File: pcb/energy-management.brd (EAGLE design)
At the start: 113.3 x 53.7 mm, 72 parts, among them J1 WIRE_HOLE-14AWG, J2 WIRE_HOLE-14AWG, J3 WIRE_HOLE-14AWG, J4 WIRE_HOLE-14AWG, U1 DS1307

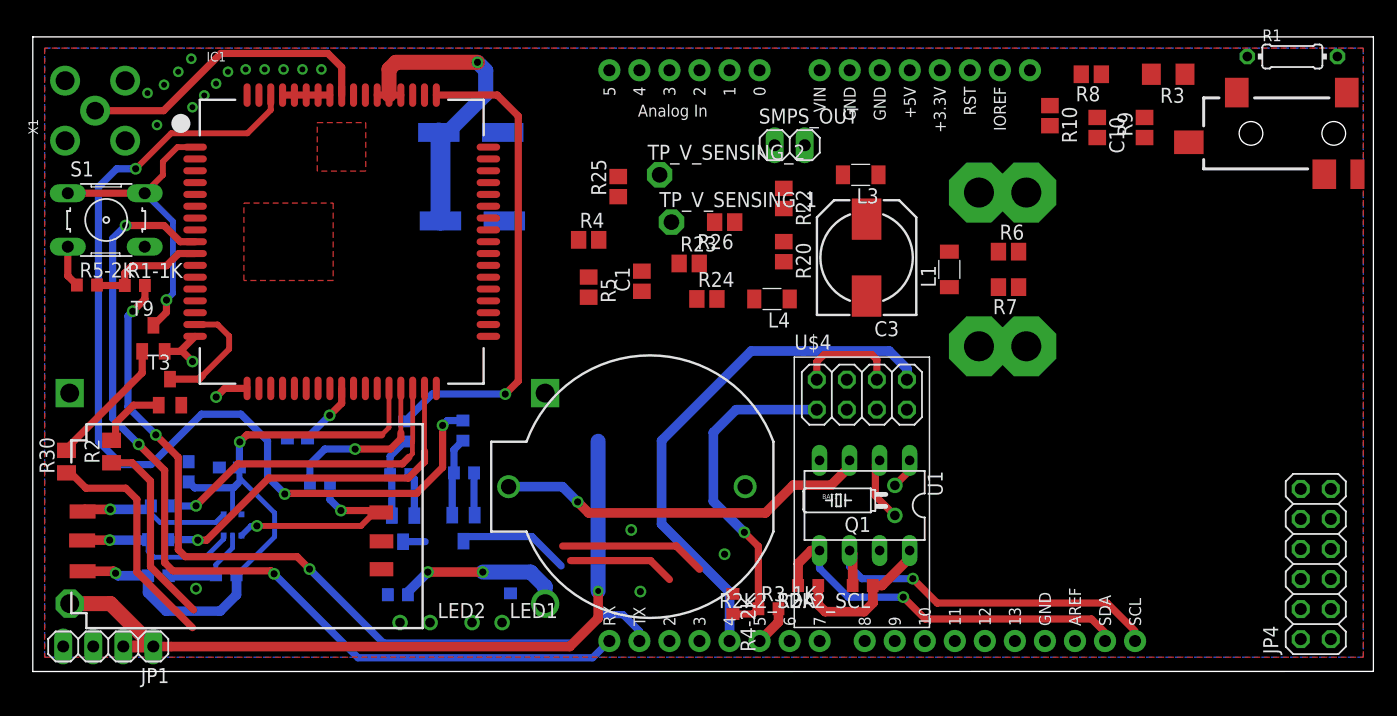
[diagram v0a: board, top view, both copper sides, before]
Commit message: added voltage and current measurement circuit
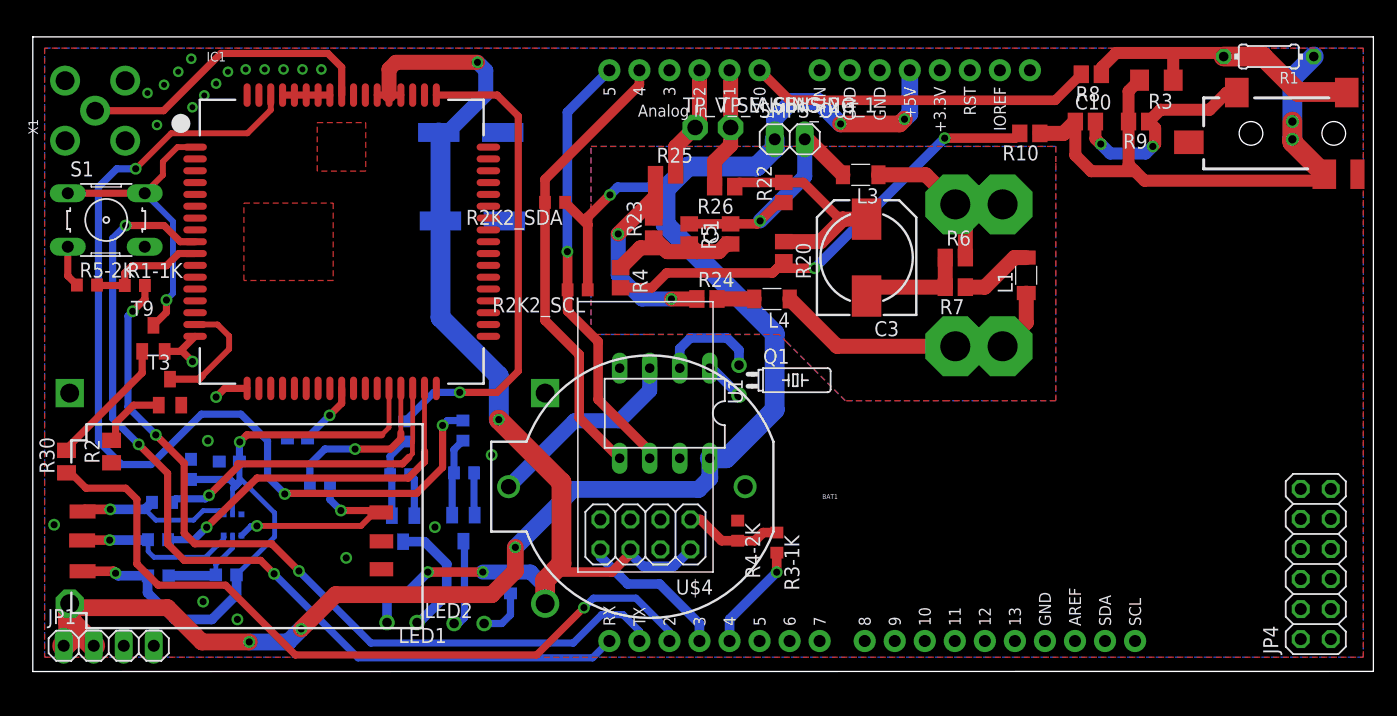
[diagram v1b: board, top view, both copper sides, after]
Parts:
- moved R2K2_SDA 38.8 mm to (44.2, 39.7)
- moved R2K2_SCL 34.7 mm to (46.1, 32.3)
- moved U$4 21.8 mm to (51.8, 11.6), turned to 180 degrees
- moved U1 18.6 mm to (53.4, 21.8)
- moved Q1 16.6 mm to (59.7, 24.6), turned to 270 degrees
- moved R5 9.62 mm to (55.5, 37.0)
- moved TP_V_SENSING_1 9.43 mm to (59.0, 46.0)
- moved C1 8.50 mm to (59.0, 37.0)
- moved L1 6.52 mm to (84.0, 33.5)
- moved R4-2K 6.21 mm to (59.6, 11.9)
- moved R3-1K 5.63 mm to (62.9, 10.9), turned to 270 degrees
- moved TP_V_SENSING_2 5.00 mm to (56.0, 46.0)
- moved R6 4.53 mm to (78.0, 35.0)
- moved R7 4.50 mm to (78.0, 32.5)
- moved R23 4.24 mm to (52.5, 37.5), turned to 90 degrees
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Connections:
- removed net 5V: SMPS_OUT.1
- net CTRL_SW1: no longer U$1.D8
- net CTRL_SW10: no longer U$1.D13
- net CTRL_SW2: no longer U$1.D9
- net CTRL_SW3: no longer U$1.D3
- net CTRL_SW4: no longer U$1.D2
- net CTRL_SW5: no longer U$1.A3
- net CTRL_SW6: no longer U$1.D7
- net CTRL_SW7: no longer U$1.D6
- net CTRL_SW8: no longer U$1.D12
- net CTRL_SW9: no longer U$1.D11
- net ESP_TX: now also U$1.D3; no longer U$1.D4
- net N$17: now also U$1.D4; no longer U$1.D5
- net PWRKEY: now also U$1.D2; no longer U$1.D10
- net VCC: now also JP1.1, JP1.2, SMPS_OUT.1, U$2.VIN
- net VIN: no longer JP1.1, JP1.2, U$2.VIN
- net V_SENSING_1: now also U$1.A1; no longer U$1.A2
- net V_SENSING_2: now also U$1.A2; no longer U$1.A1
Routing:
- net VCC: track 13.0 -> 148.5 mm, vias 0 -> 6
- net VIN: track 64.7 -> 0.00 mm, vias 1 -> 0
- net N$26: track 0.00 -> 50.0 mm, vias 0 -> 2
- net +3V3: track 53.9 -> 97.3 mm, vias 3 -> 4
- net 3V3: track 0.00 -> 39.9 mm, vias 0 -> 2
- net PWRKEY: track 28.7 -> 64.5 mm, vias 0 -> 1
- net ESP_TX: track 44.9 -> 12.8 mm
- net I_SENSING: track 0.00 -> 29.2 mm
- net RESET: track 28.7 -> 0.00 mm
- net N$25: track 0.00 -> 25.5 mm
- net WALL_PHASE: track 0.00 -> 25.0 mm
- net GND: track 30.1 -> 51.8 mm, vias 21 -> 25
- net ESP_RX: track 28.4 -> 8.33 mm, vias 1 -> 0
- net N$21: track 0.00 -> 19.1 mm, vias 0 -> 2
- net N$24: track 0.00 -> 18.4 mm
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- added copper zone on layer 1, net N$27
- added copper zone on layer 16, net N$28

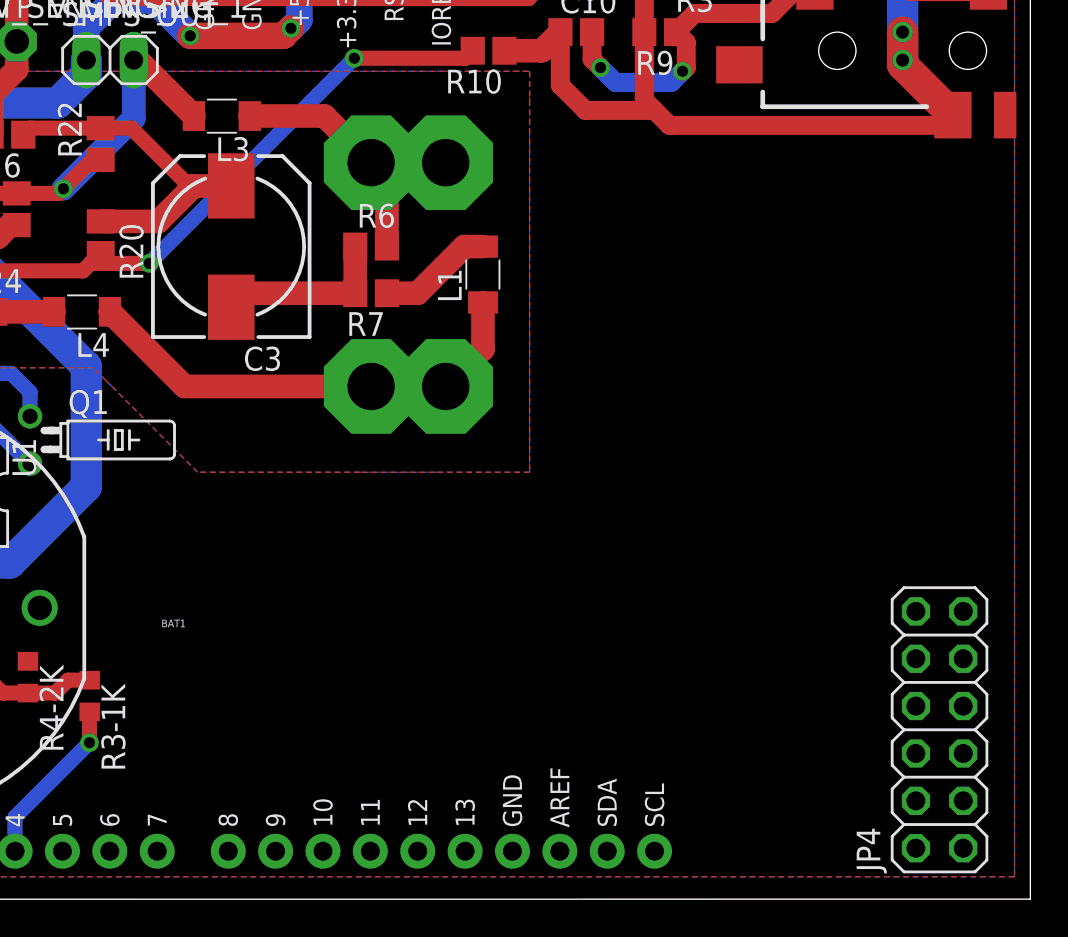
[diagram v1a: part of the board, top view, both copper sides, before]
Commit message: routing shift register
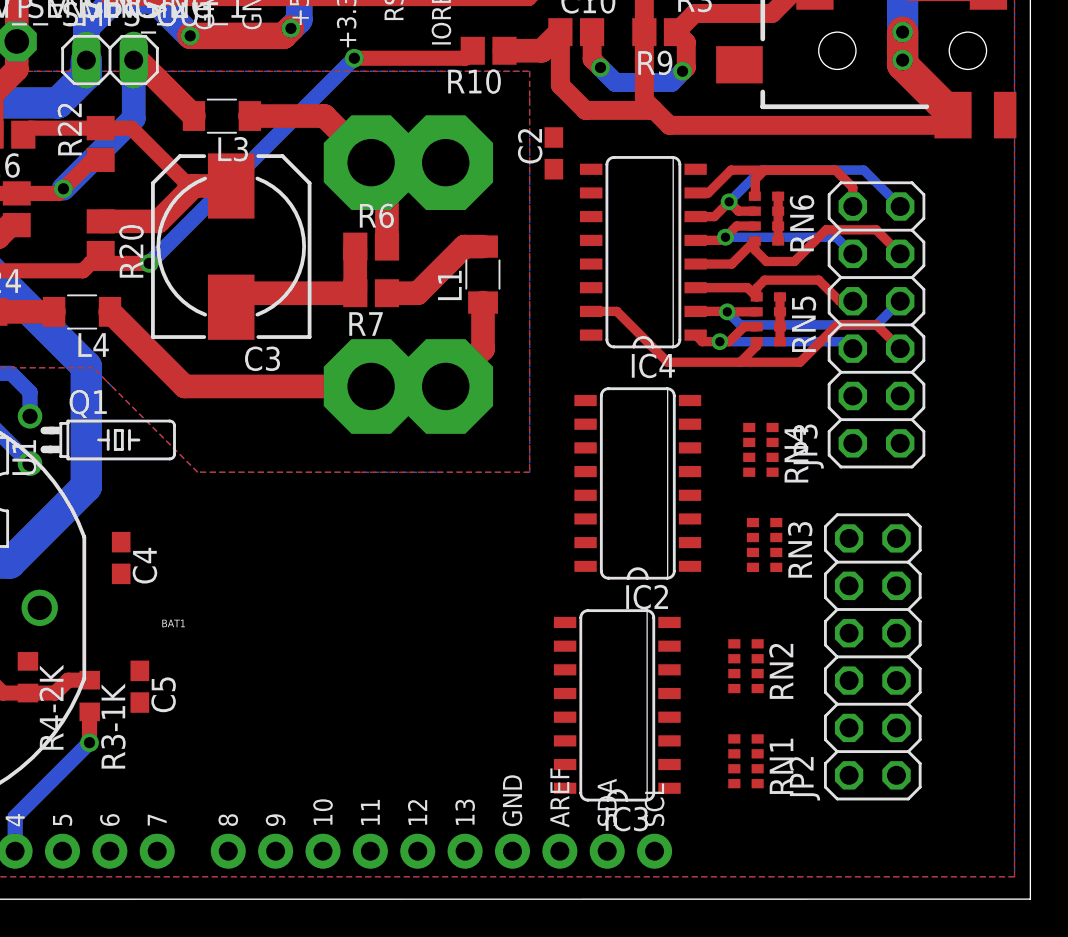
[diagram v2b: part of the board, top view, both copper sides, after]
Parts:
- removed JP4: (no value), pinhead:2X06
- added C2, C4, C5: (no value), rcl:C0603
- added IC2, IC3, IC4: 74LS595D, SparkFun-DigitalIC:SO16
- added JP2, JP3: (no value), pinhead:2X06
- added RN1, RN2, RN3, RN4, RN5, RN6: (no value), resistor-dil:0603-ARC
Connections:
- removed net CTRL_SW1: JP4.4
- removed net CTRL_SW10: JP4.7
- removed net CTRL_SW2: JP4.2
- removed net CTRL_SW3: JP4.1
- removed net CTRL_SW4: JP4.3
- removed net CTRL_SW5: JP4.5
- removed net CTRL_SW6: JP4.6
- removed net CTRL_SW7: JP4.8
- removed net CTRL_SW8: JP4.10
- removed net CTRL_SW9: JP4.9
- new net DS: IC3.14, U$1.D11
- new net N$29: IC2.14, IC3.9
- new net N$30: IC2.9, IC4.14
- new net OUT_1: IC3.15, JP2.1, RN1.1
- new net OUT_10: IC2.1, JP2.10, RN3.2
- new net OUT_11: IC2.2, JP2.11, RN3.3
- new net OUT_12: IC2.3, JP2.12, RN3.4
- new net OUT_13: IC2.4, JP3.1, RN4.1
- new net OUT_14: IC2.5, JP3.2, RN4.2
- new net OUT_15: IC2.6, JP3.3, RN4.3
- new net OUT_16: IC2.7, JP3.4, RN4.4
- new net OUT_17: IC4.15, JP3.5, RN5.8
- new net OUT_18: IC4.1, JP3.6, RN5.7
- new net OUT_19: IC4.2, JP3.7, RN5.6
- new net OUT_2: IC3.1, JP2.2, RN1.2
- new net OUT_20: IC4.3, JP3.8, RN5.5
- new net OUT_21: IC4.4, JP3.9, RN6.8
- new net OUT_22: IC4.5, JP3.10, RN6.7
- new net OUT_23: IC4.6, JP3.11, RN6.6
- new net OUT_24: IC4.7, JP3.12, RN6.5
- new net OUT_3: IC3.2, JP2.3, RN1.3
- new net OUT_4: IC3.3, JP2.4, RN1.4
- new net OUT_5: IC3.4, JP2.5, RN2.1
- new net OUT_6: IC3.5, JP2.6, RN2.2
- new net OUT_7: IC3.6, JP2.7, RN2.3
- new net OUT_8: IC3.7, JP2.8, RN2.4
- new net OUT_9: IC2.15, JP2.9, RN3.1
- new net SH_CP: IC2.11, IC3.11, IC4.11, U$1.D12
- new net ST_CP: C2.1, C4.1, C5.1, IC2.12, IC3.12, IC4.12, U$1.D8
- net GND: now also C2.2, C4.2, C5.2, IC2.13, IC2.8, IC3.13, IC3.8, IC4.13, IC4.8
- net VCC: now also IC2.10, IC2.16, IC3.10, IC3.16, IC4.10, IC4.16, RN1.5, RN1.6, RN1.7, RN1.8, RN2.5, RN2.6, RN2.7, RN2.8, RN3.5, RN3.6, RN3.7, RN3.8, RN4.5, RN4.6, RN4.7, RN4.8, RN5.1, RN5.2, RN5.3, RN5.4, RN6.1, RN6.2, RN6.3, RN6.4; no longer JP4.11, JP4.12
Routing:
- net OUT_17: track 0.00 -> 20.5 mm
- net OUT_23: track 0.00 -> 14.4 mm, vias 0 -> 1
- net OUT_21: track 0.00 -> 13.5 mm
- net OUT_19: track 0.00 -> 13.4 mm, vias 0 -> 1
- net OUT_24: track 0.00 -> 12.0 mm
- net OUT_18: track 0.00 -> 11.0 mm, vias 0 -> 1
- net OUT_22: track 0.00 -> 10.7 mm, vias 0 -> 1
- net OUT_20: track 0.00 -> 9.75 mm
- net VCC: track 148.5 -> 153.3 mm

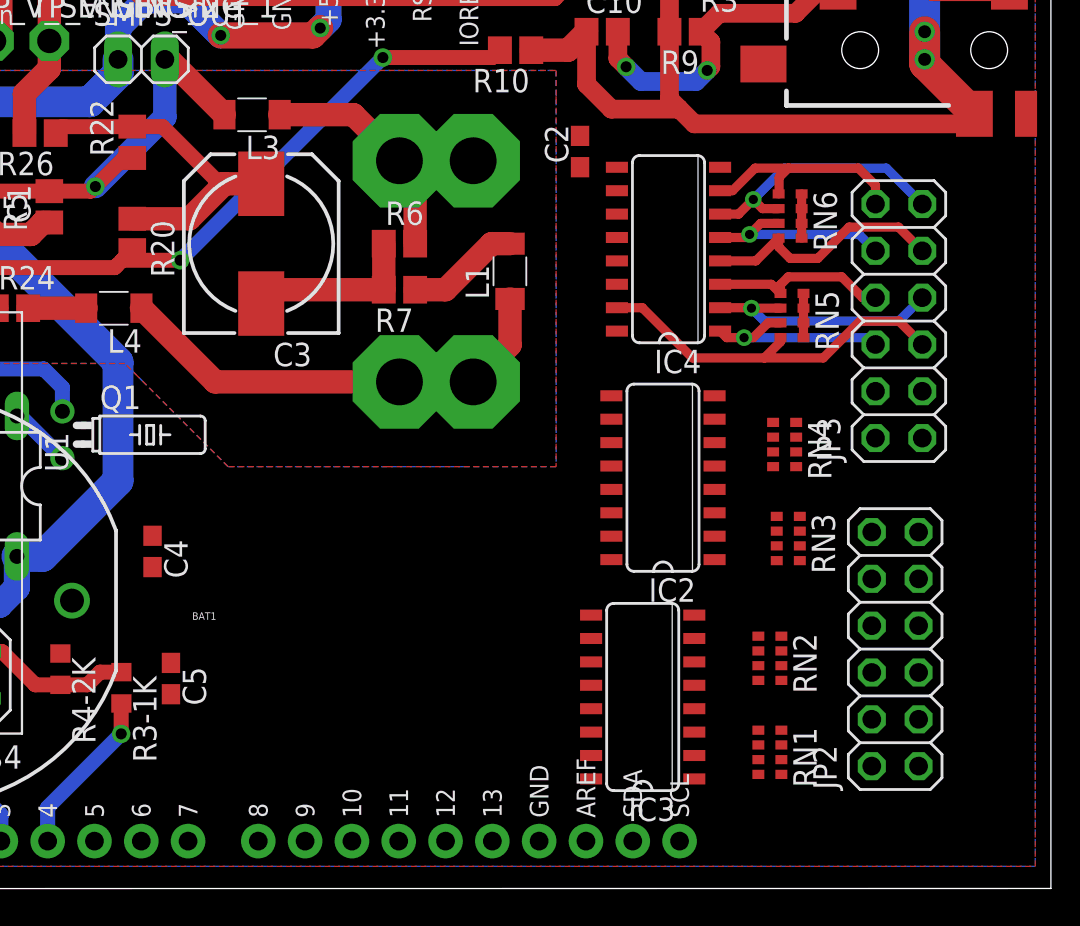
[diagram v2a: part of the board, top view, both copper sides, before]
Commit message: pcb with shift register and dht22
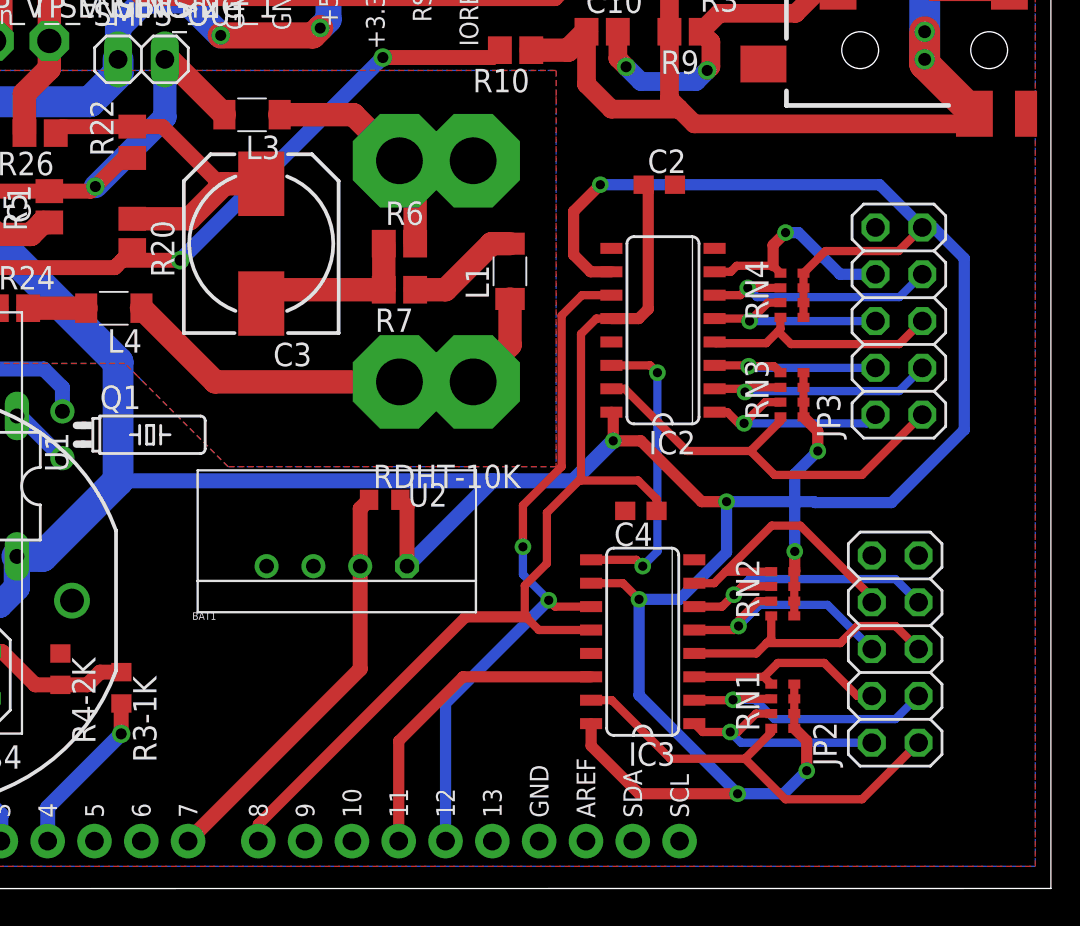
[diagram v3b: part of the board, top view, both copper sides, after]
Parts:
- removed C5: (no value), rcl:C0603
- removed IC4: 74LS595D, SparkFun-DigitalIC:SO16
- removed RN5, RN6: (no value), resistor-dil:0603-ARC
- added RDHT-10K: (no value), rcl:R0603
- added U2: (no value), RHT03_DHT-22_AM2302:RHT03_DHT-22
- JP2, JP3: device pinhead:2X06 -> pinhead:2X05
- moved C4 26.6 mm to (91.1, 20.5), turned to 180 degrees
- moved RN4 8.11 mm to (99.3, 32.2), turned to 270 degrees
- moved IC2 8.00 mm to (92.3, 30.3)
- moved RN3 7.80 mm to (99.3, 26.8), turned to 270 degrees
- moved C2 4.66 mm to (92.1, 38.2), turned to 0 degrees
- moved RN2 3.57 mm to (98.8, 16.0), turned to 270 degrees
- moved IC3 3.00 mm to (91.2, 13.4)
- moved RN1 2.60 mm to (98.8, 9.90), turned to 270 degrees
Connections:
- removed net OUT_17: IC4.15, JP3.5, RN5.8
- removed net OUT_18: IC4.1, JP3.6, RN5.7
- removed net OUT_19: IC4.2, JP3.7, RN5.6
- removed net OUT_20: IC4.3, JP3.8, RN5.5
- removed net OUT_21: IC4.4, JP3.9, RN6.8
- removed net OUT_22: IC4.5, JP3.10, RN6.7
- removed net OUT_23: IC4.6, JP3.11, RN6.6
- removed net OUT_24: IC4.7, JP3.12, RN6.5
- new net DHT_DATA: RDHT-10K.1, U$1.D7, U2.DATA
- new net N$32: U2.NULL
- net GND: now also JP2.10, JP3.10, U2.GND; no longer C5.2, IC4.13, IC4.8
- net N$30: now also JP2.9; no longer IC2.9, IC4.14
- net OUT_1: now also RN1.4; no longer RN1.1
- net OUT_10: now also JP3.2, RN3.3; no longer JP2.10, RN3.2
- net OUT_11: now also JP3.3, RN3.2; no longer JP2.11, RN3.3
- net OUT_12: now also JP3.4, RN3.1; no longer JP2.12, RN3.4
- net OUT_13: now also JP3.5, RN4.4; no longer JP3.1, RN4.1
- net OUT_14: now also JP3.6, RN4.3; no longer JP3.2, RN4.2
- net OUT_15: now also JP3.7, RN4.2; no longer JP3.3, RN4.3
- net OUT_16: now also JP3.8, RN4.1; no longer JP3.4, RN4.4
- net OUT_2: now also RN1.3; no longer RN1.2
- net OUT_3: now also RN1.2; no longer RN1.3
- net OUT_4: now also RN1.1; no longer RN1.4
- net OUT_5: now also RN2.4; no longer RN2.1
- net OUT_6: now also RN2.3; no longer RN2.2
- net OUT_7: now also RN2.2; no longer RN2.3
- net OUT_8: now also RN2.1; no longer RN2.4
- net OUT_9: now also JP3.1, RN3.4; no longer JP2.9, RN3.1
- net SH_CP: no longer IC4.11
- net ST_CP: no longer C5.1, IC4.12
- net VCC: now also JP3.9, RDHT-10K.2, U2.VDD; no longer IC4.10, IC4.16, RN5.1, RN5.2, RN5.3, RN5.4, RN6.1, RN6.2, RN6.3, RN6.4
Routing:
- net VCC: track 153.3 -> 315.5 mm, vias 6 -> 14
- net ST_CP: track 0.00 -> 56.9 mm
- net SH_CP: track 0.00 -> 37.9 mm, vias 0 -> 2
- net OUT_1: track 0.00 -> 23.5 mm
- net OUT_9: track 0.00 -> 22.7 mm
- net DHT_DATA: track 0.00 -> 22.6 mm
- net OUT_17: track 20.5 -> 0.00 mm
- net DS: track 0.00 -> 17.3 mm
- net N$29: track 0.00 -> 16.4 mm, vias 0 -> 2
- net OUT_7: track 0.00 -> 15.5 mm, vias 0 -> 1
- net OUT_8: track 0.00 -> 15.3 mm
- net OUT_3: track 0.00 -> 15.2 mm, vias 0 -> 1
- net OUT_5: track 0.00 -> 14.9 mm
- net OUT_23: track 14.4 -> 0.00 mm, vias 1 -> 0
- net OUT_15: track 0.00 -> 13.9 mm, vias 0 -> 1
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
